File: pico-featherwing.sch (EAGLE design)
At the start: 3 parts, among them U1 RASPBERRY_PICOSMD-TH

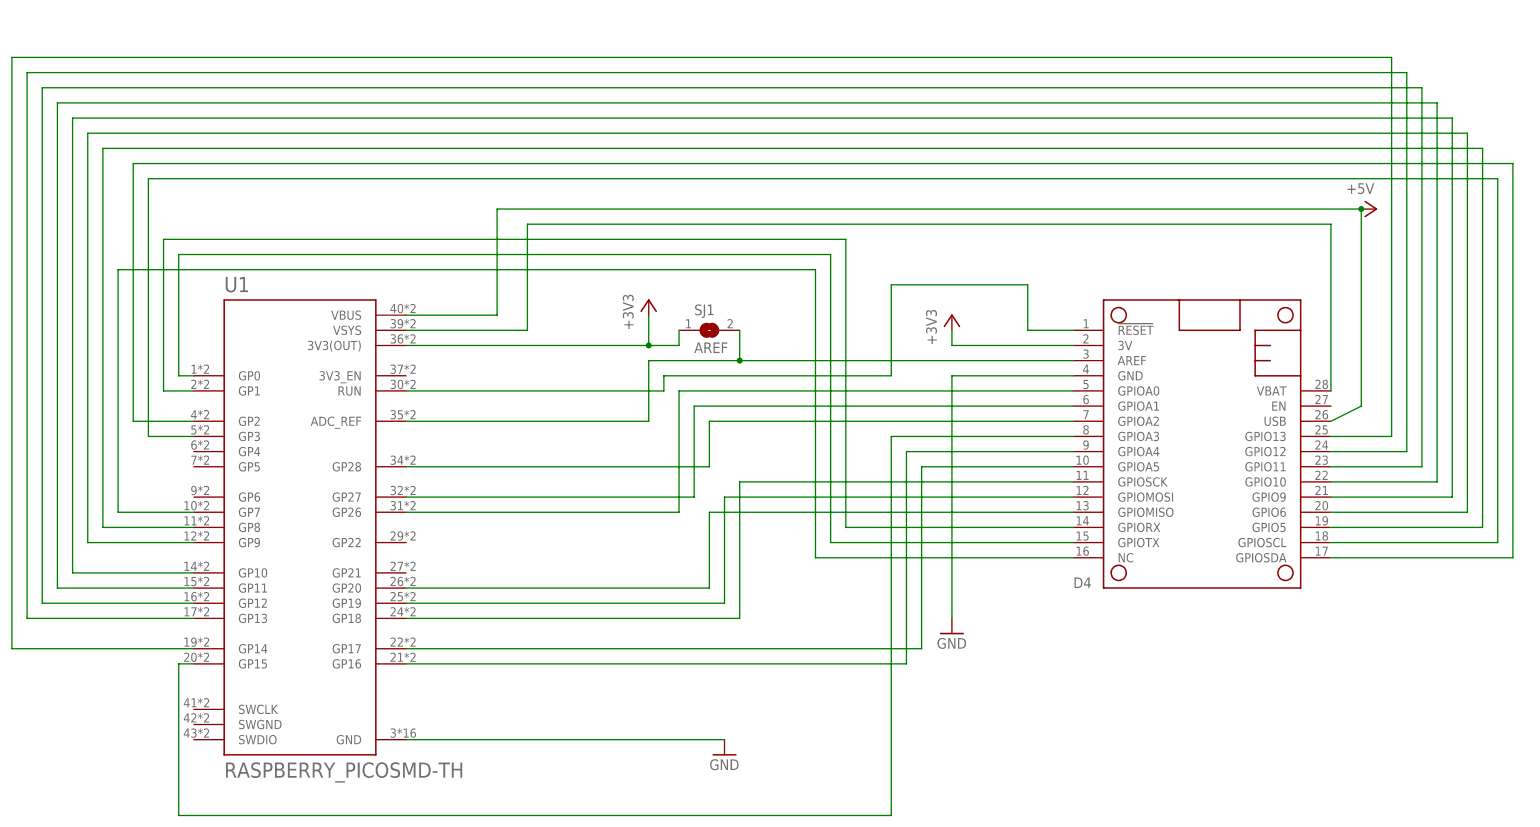
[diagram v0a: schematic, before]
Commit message: Fixed pinouts, etc.
Improved ground plane and connections.
Removed ADC ref pads.
Improved 3V3 connections on FeatherWing side.
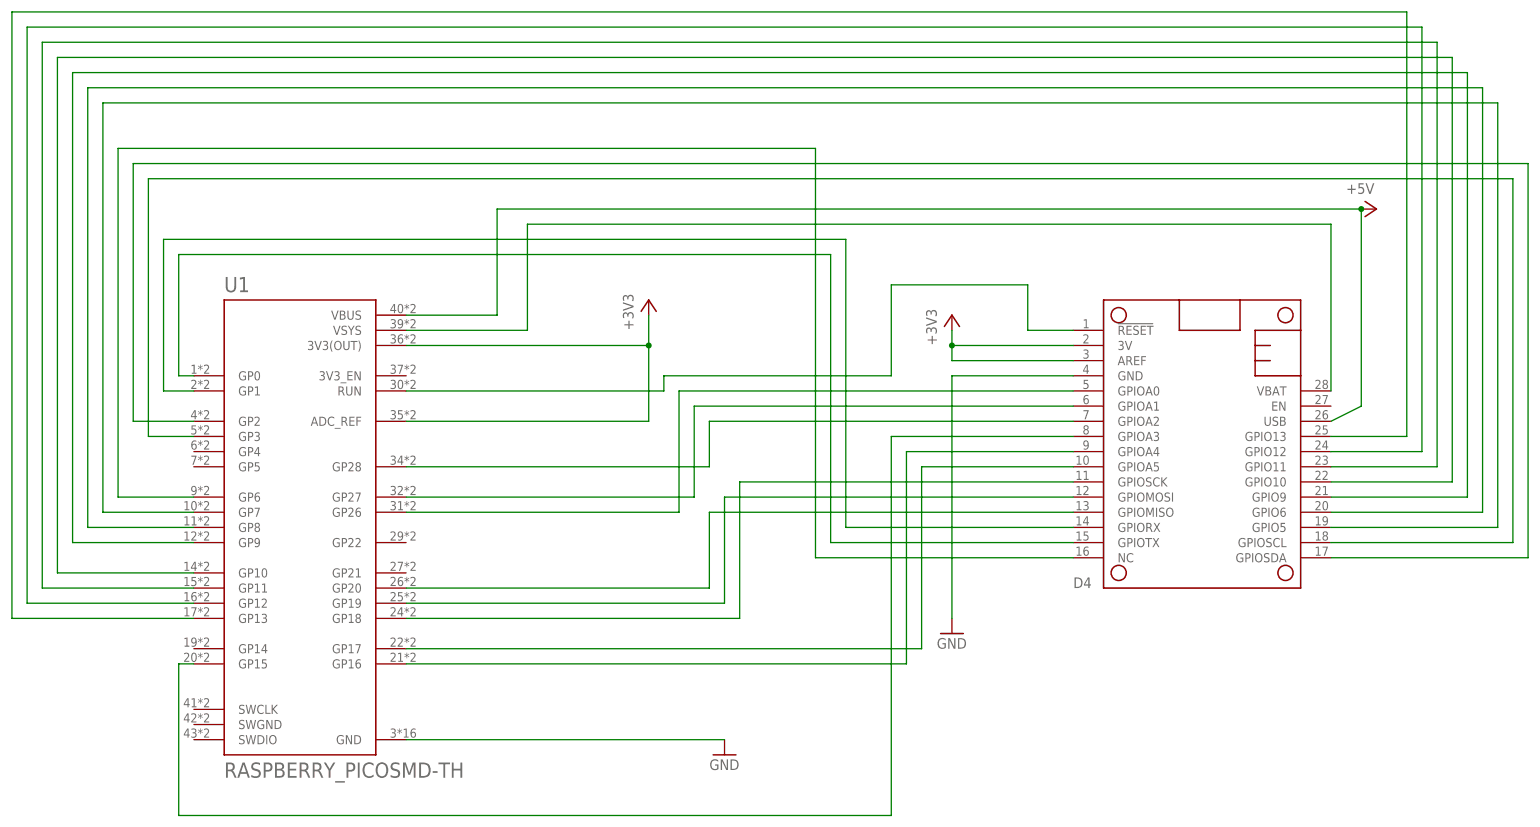
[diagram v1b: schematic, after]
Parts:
- removed SJ1: AREF, jumper:SJW
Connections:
- removed net N$20: MS1.AREF, SJ1.2, U1.ADC_REF
- net +3V3: now also MS1.AREF, U1.ADC_REF; no longer SJ1.1
- net D4: now also MS1.GPIO5; no longer MS1.NC
- net N$3: now also MS1.GPIO6; no longer MS1.GPIO5
- net N$4: now also MS1.GPIO9; no longer MS1.GPIO6
- net N$5: now also MS1.GPIO10; no longer MS1.GPIO9
- net N$6: now also MS1.GPIO11; no longer MS1.GPIO10
- net N$7: now also MS1.GPIO12; no longer MS1.GPIO11
- net N$8: now also MS1.GPIO13; no longer MS1.GPIO12
- net N$9: now also MS1.NC, U1.GP6; no longer MS1.GPIO13, U1.GP14
